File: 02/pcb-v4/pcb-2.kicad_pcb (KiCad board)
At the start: 2 copper layers, 146.9 x 86 mm, 44 parts, among them U1 Arduino_Pro_Micro, U2 TRRS

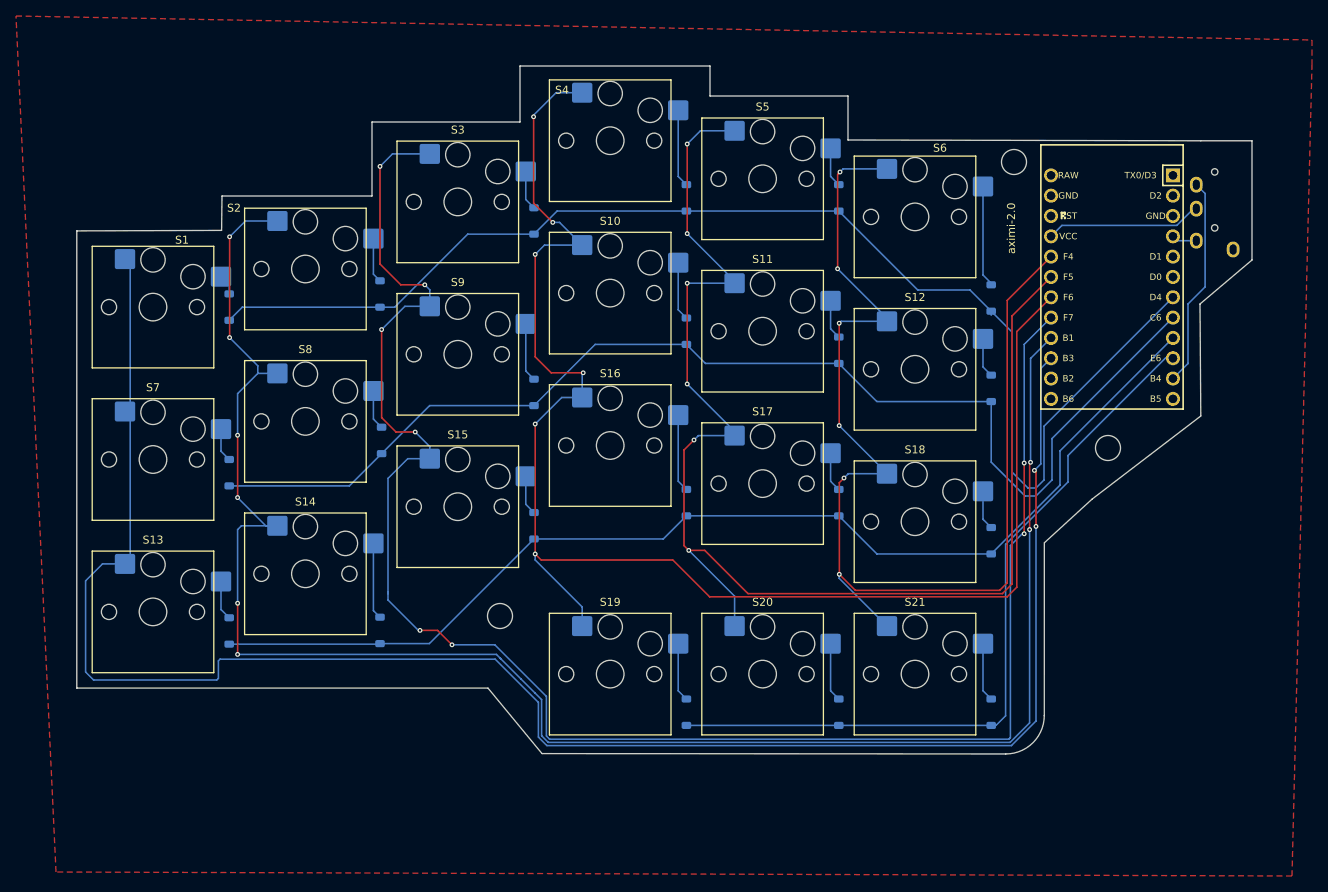
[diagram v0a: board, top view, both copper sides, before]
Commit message: feat: swap all 21 switch footprints to reversible Choc V1 hotswap
Replaced every PCM_Switch_Keyboard_Hotswap_Kailh:SW_Hotswap_Kailh_Choc_V1
footprint in pcb-v4 with Library:Kailh_socket_PG1350_reversible. Each switch
now has pads 1 & 2 on both F.Cu and B.Cu, allowing the hotswap socket to be
soldered on either side of the board so one PCB serves as either half.

Net assignments and positions preserved; traces to old pad positions will flag
as DRC errors — re-route in KiCad before generating Gerbers.

Co-Authored-By: Claude Sonnet 4.6 <noreply@anthropic.com>
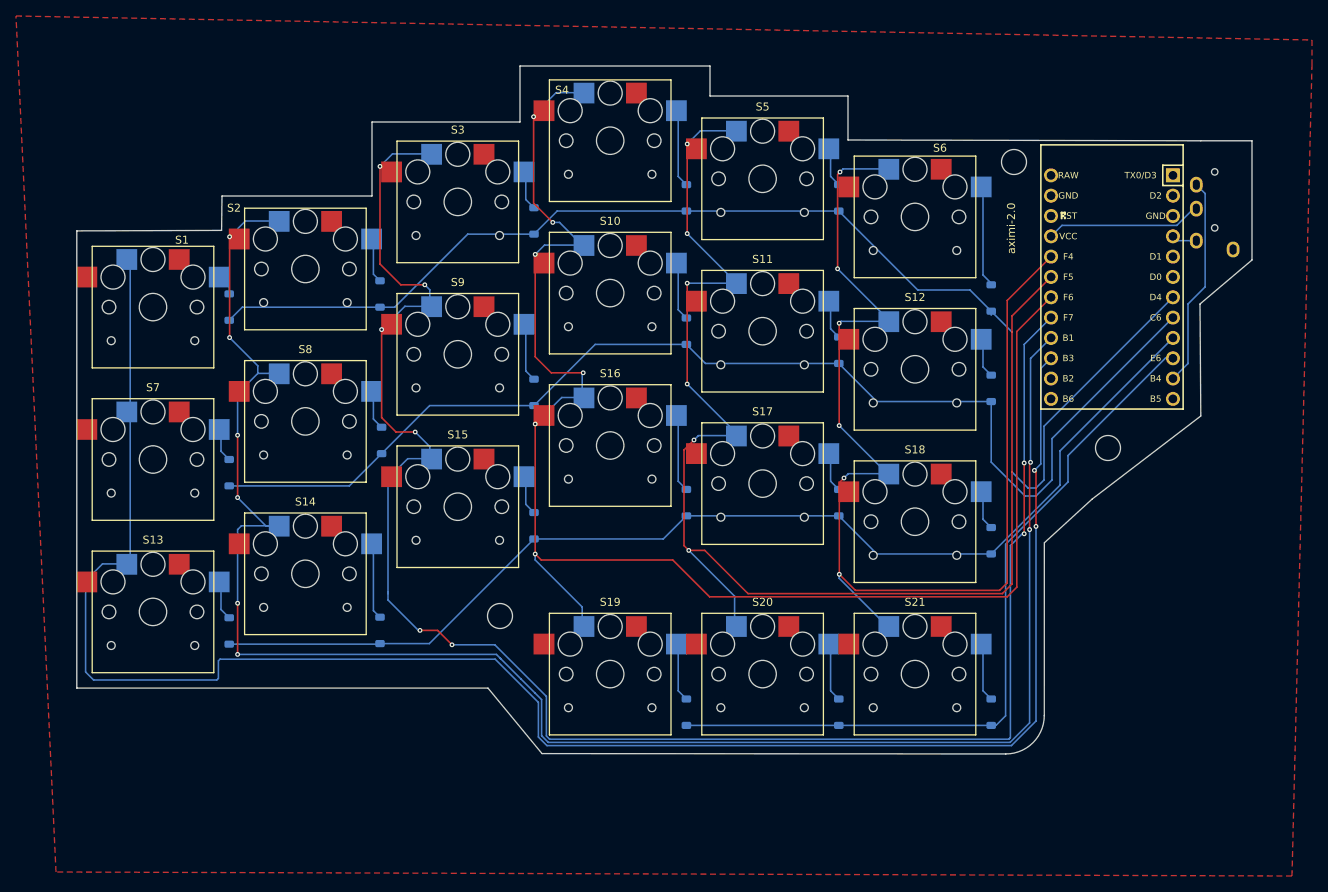
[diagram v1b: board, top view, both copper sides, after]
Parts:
- S1, S10, S11, S12, S13, S14, S15, S16, S17, S18, S19, S2, S20, S21, S3, S4, S5, S6, S7, S8, S9: footprint PCM_Switch_Keyboard_Hotswap_Kailh:SW_Hotswap_Kailh_Choc_V1 -> Library:Kailh_socket_PG1350_reversible

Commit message: feat: swap all 21 diodes to reversible SOD-123 footprint
Added Library:Diode_SOD-123_reversible to Library.pretty — pads 1 (K)
and 2 (A) are present on both F.Cu and B.Cu at the same positions,
with mirrored F.SilkS polarity marks and F.CrtYd courtyard.

Replaced every Scotto Components:Diode_SOD-123 footprint in pcb-v4
with the reversible variant. Net assignments (Row X, Net-(DX-A)) are
preserved; traces will need re-routing in KiCad.

Co-Authored-By: Claude Sonnet 4.6 <noreply@anthropic.com>
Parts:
- D1, D10, D11, D12, D13, D14, D15, D16, D17, D18, D19, D2, D20, D21, D3, D4, D5, D6, D7, D8, D9: footprint Scotto Components:Diode_SOD-123 -> Library:Diode_SOD-123_reversible

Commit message: fix: reversible footprints — schematic sync, TRRS, DRC flags
- Updated pcb-2.kicad_sch: all 21 diodes, 21 switches, and TRRS now
  reference Library:* footprints so KiCad won't revert them on re-open
- Added Library:TRRS_PJ-320A_reversible with F.SilkS + B.SilkS body
  outline and F.CrtYd + B.CrtYd courtyard (TH pads already *.Cu)
- Re-ran diode swap (KiCad had reverted to Scotto library versions)
- Set duplicate_pad_numbers_are_jumpers yes on all 42 reversible
  footprints (switches + diodes) — fixes the DRC duplicate-pad errors

Co-Authored-By: Claude Sonnet 4.6 <noreply@anthropic.com>
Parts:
- U2: footprint ScottoKeebs_Components:TRRS_PJ-320A -> Library:TRRS_PJ-320A_reversible
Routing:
- net Column 1: track 231.5 -> 419.4 mm, vias 2 -> 7
- net Column 2: track 230.3 -> 402.4 mm, vias 8 -> 13
- net Column 3: track 220.6 -> 337.1 mm, vias 8 -> 13
- net Column 4: track 191.8 -> 276.8 mm, vias 6 -> 13
- net Column 5: track 170.3 -> 245.5 mm, vias 6 -> 12
- net Column 6: track 147.3 -> 218.6 mm, vias 6 -> 11
